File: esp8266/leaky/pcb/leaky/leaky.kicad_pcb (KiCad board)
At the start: 2 copper layers, 100 x 100 mm, 31 parts, among them J1 UART, J2 extra pins, Q1 BC327, SW1 sensing loop, U1 DD0405MA, U2 ESP-12F

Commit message: leaky: Add bot sensing
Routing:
- net Net-(R1-Pad2): track 1490.2 -> 2970.3 mm
- net GND: track 1524.2 -> 2990.4 mm

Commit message: leaky: Add logo
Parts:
- added G***: LOGO, _my:logo, F.Cu at (65.5, 47.2)
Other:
- board text added: "JLCJLCJLCJLC"
- board text added: "https://github.com/tantecky/embedded"
- board text added: "v1.0"

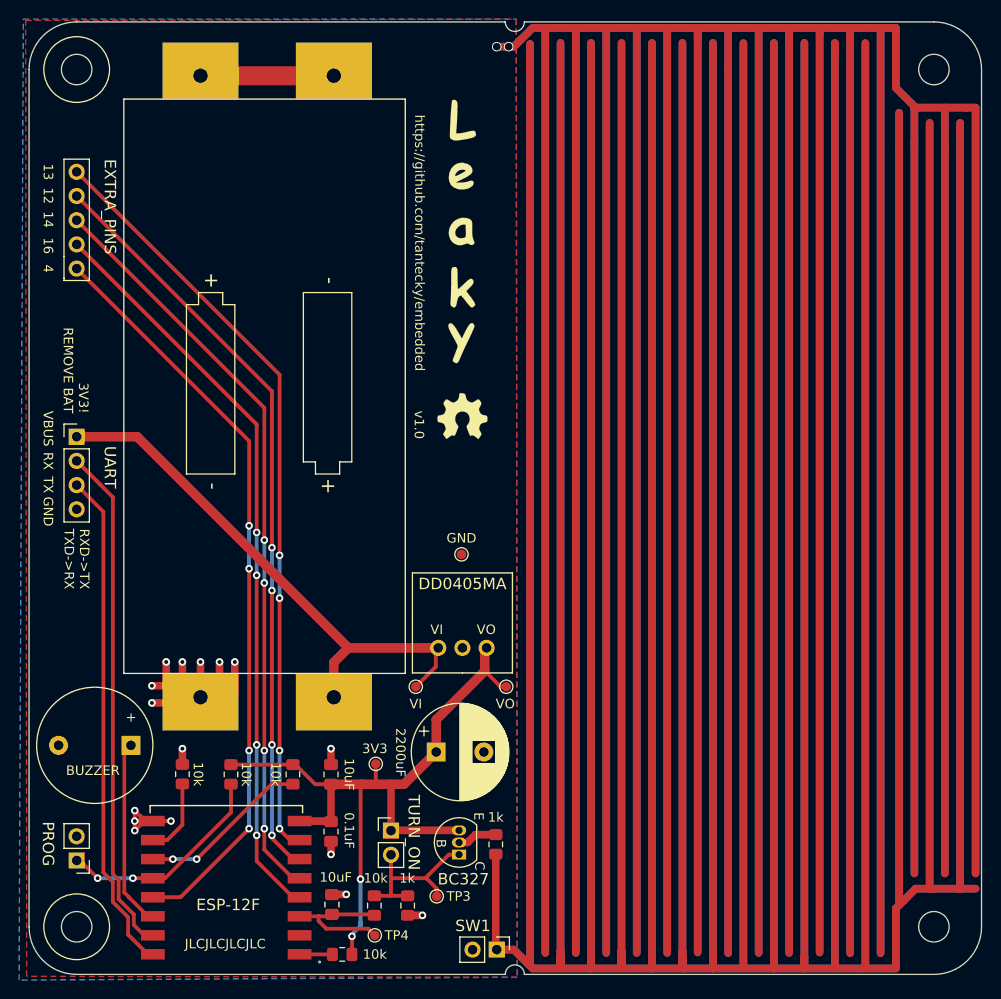
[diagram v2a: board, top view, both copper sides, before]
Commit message: leaky: Add stiching vias
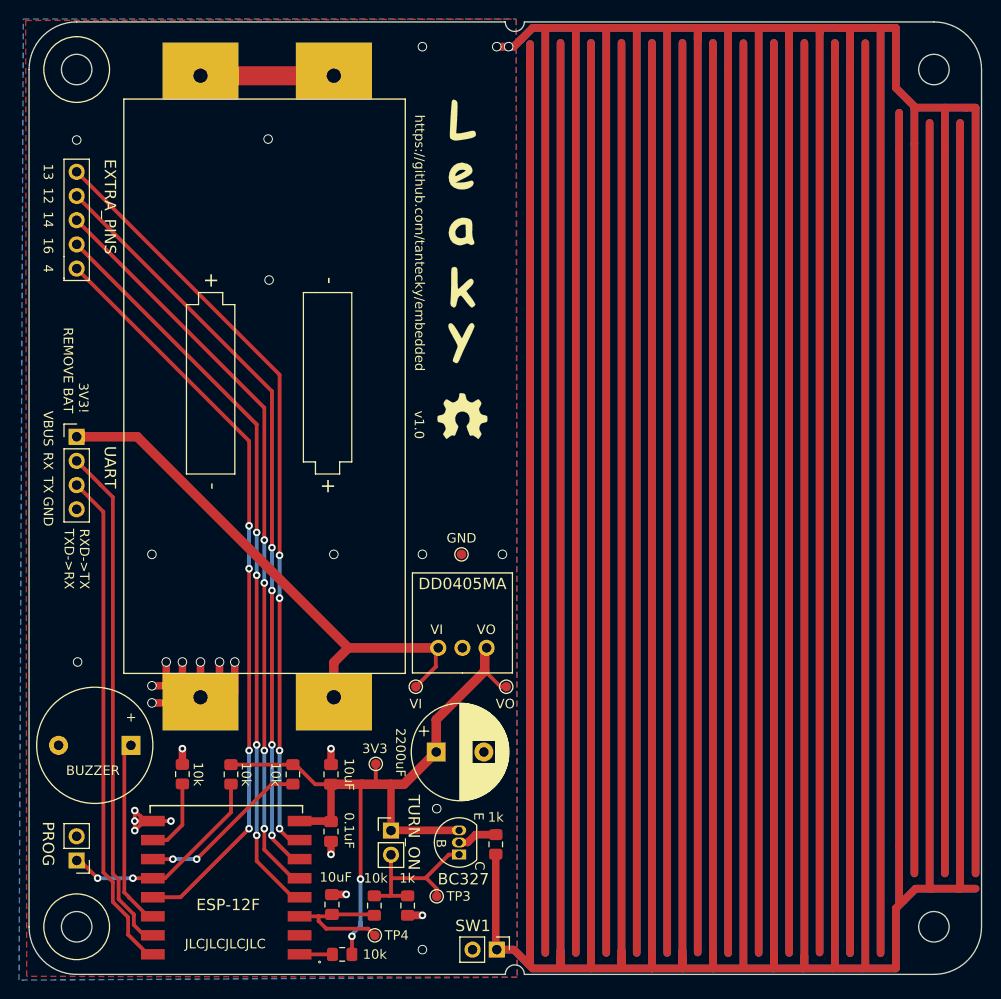
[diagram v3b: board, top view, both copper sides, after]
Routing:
- net GND: vias 18 -> 29

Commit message: leaky: Small tweaks
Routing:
- net GND: track 2990.4 -> 2991.6 mm

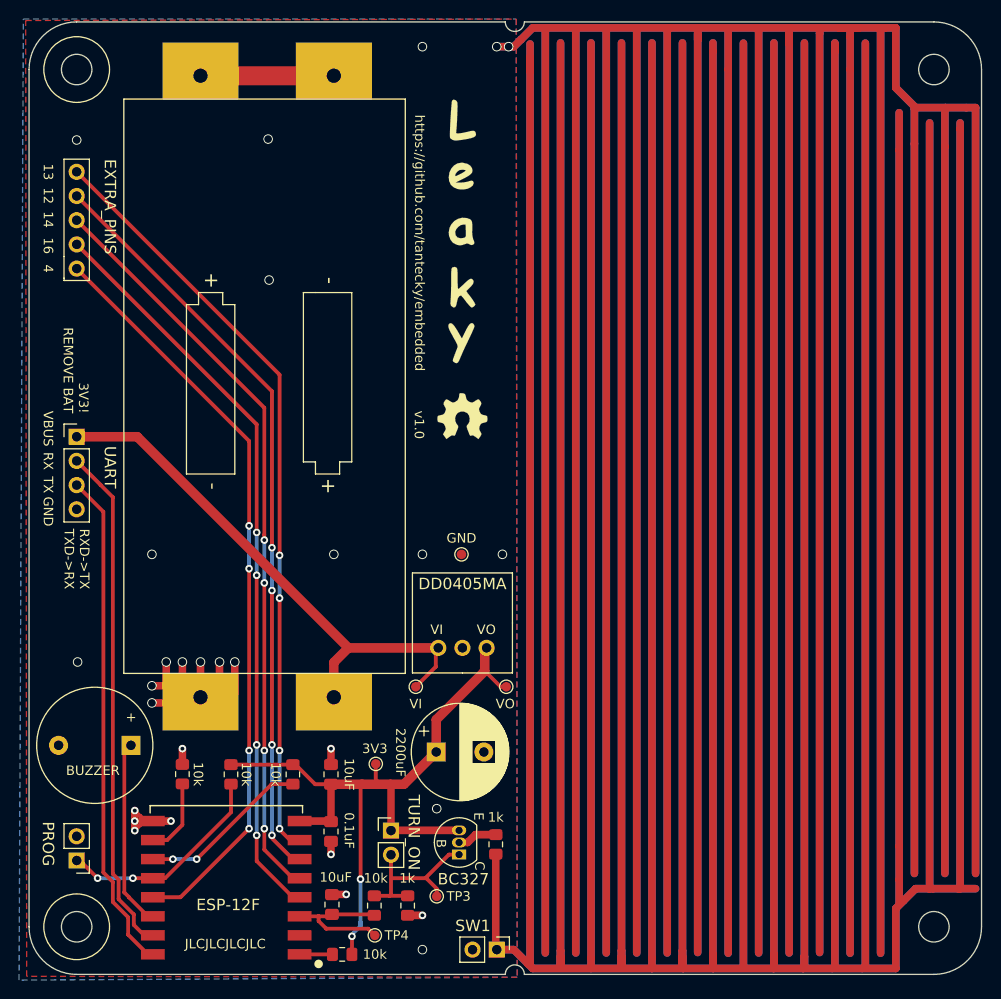
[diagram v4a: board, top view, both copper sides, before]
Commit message: leaky: Small adjustments
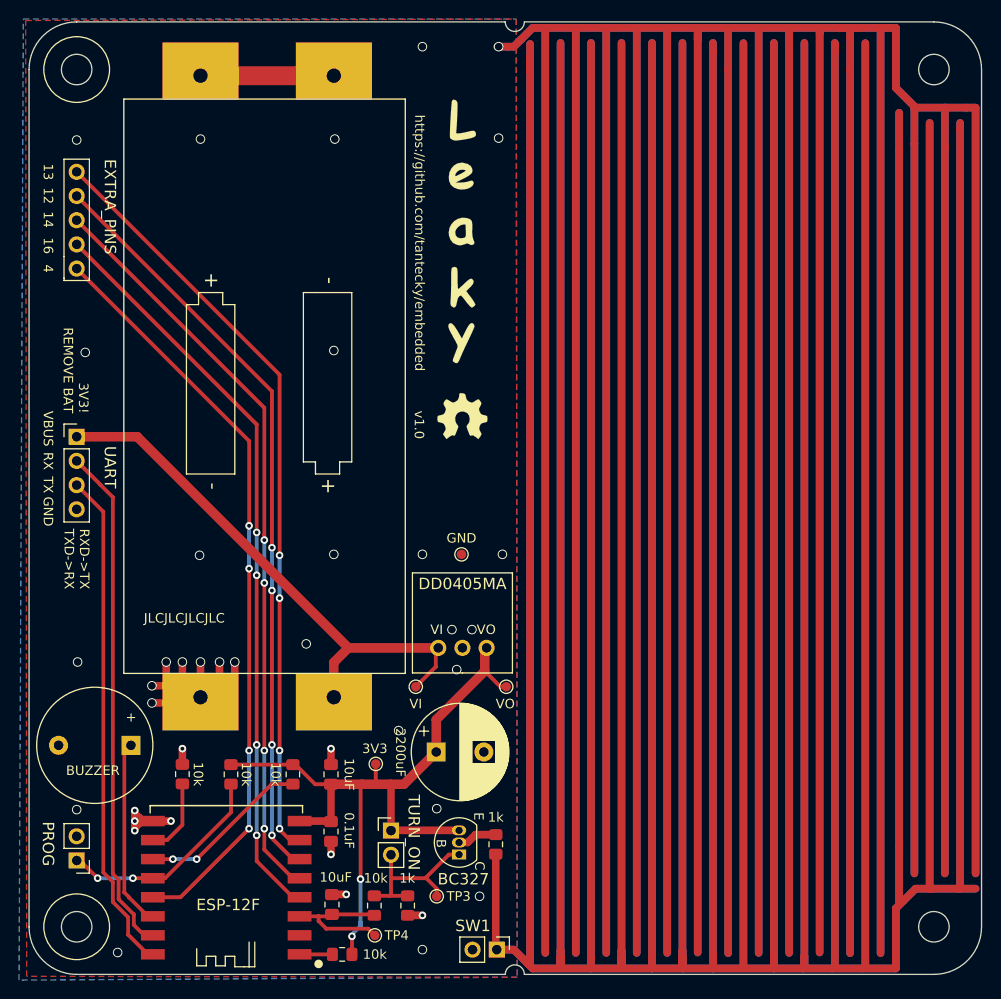
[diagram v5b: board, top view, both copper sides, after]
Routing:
- net GND: vias 29 -> 39

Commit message: leaky: Send v1.0 to jlcpcb
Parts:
- moved TP1 0.70 mm to (65.4, 75.2)
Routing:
- net Net-(R1-Pad2): track 2970.3 -> 2972.2 mm
